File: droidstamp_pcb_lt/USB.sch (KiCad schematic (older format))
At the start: 41 parts, among them J2 USB_2A, J3 USB_2A, P4 CONN_4X2, U4 GL850G, U5 RCLAMP0502B, U6 RCLAMP0502B, U7 RCLAMP0502B, U8 RCLAMP0502B, X2 12MHz

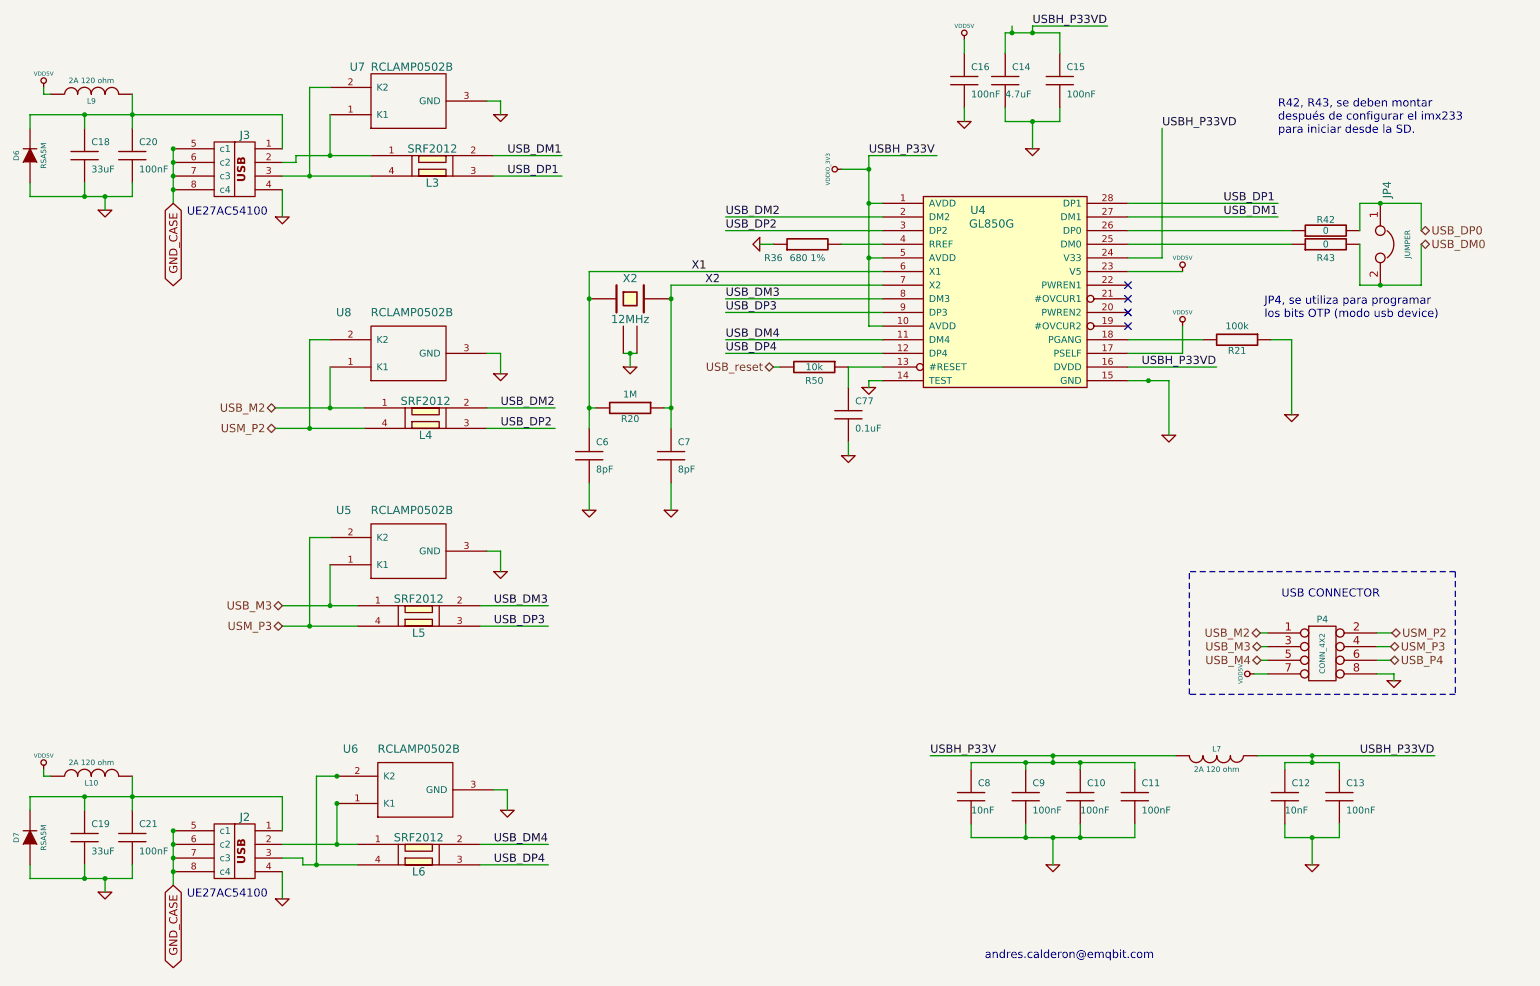
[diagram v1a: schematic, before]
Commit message: USB PC compatible connector
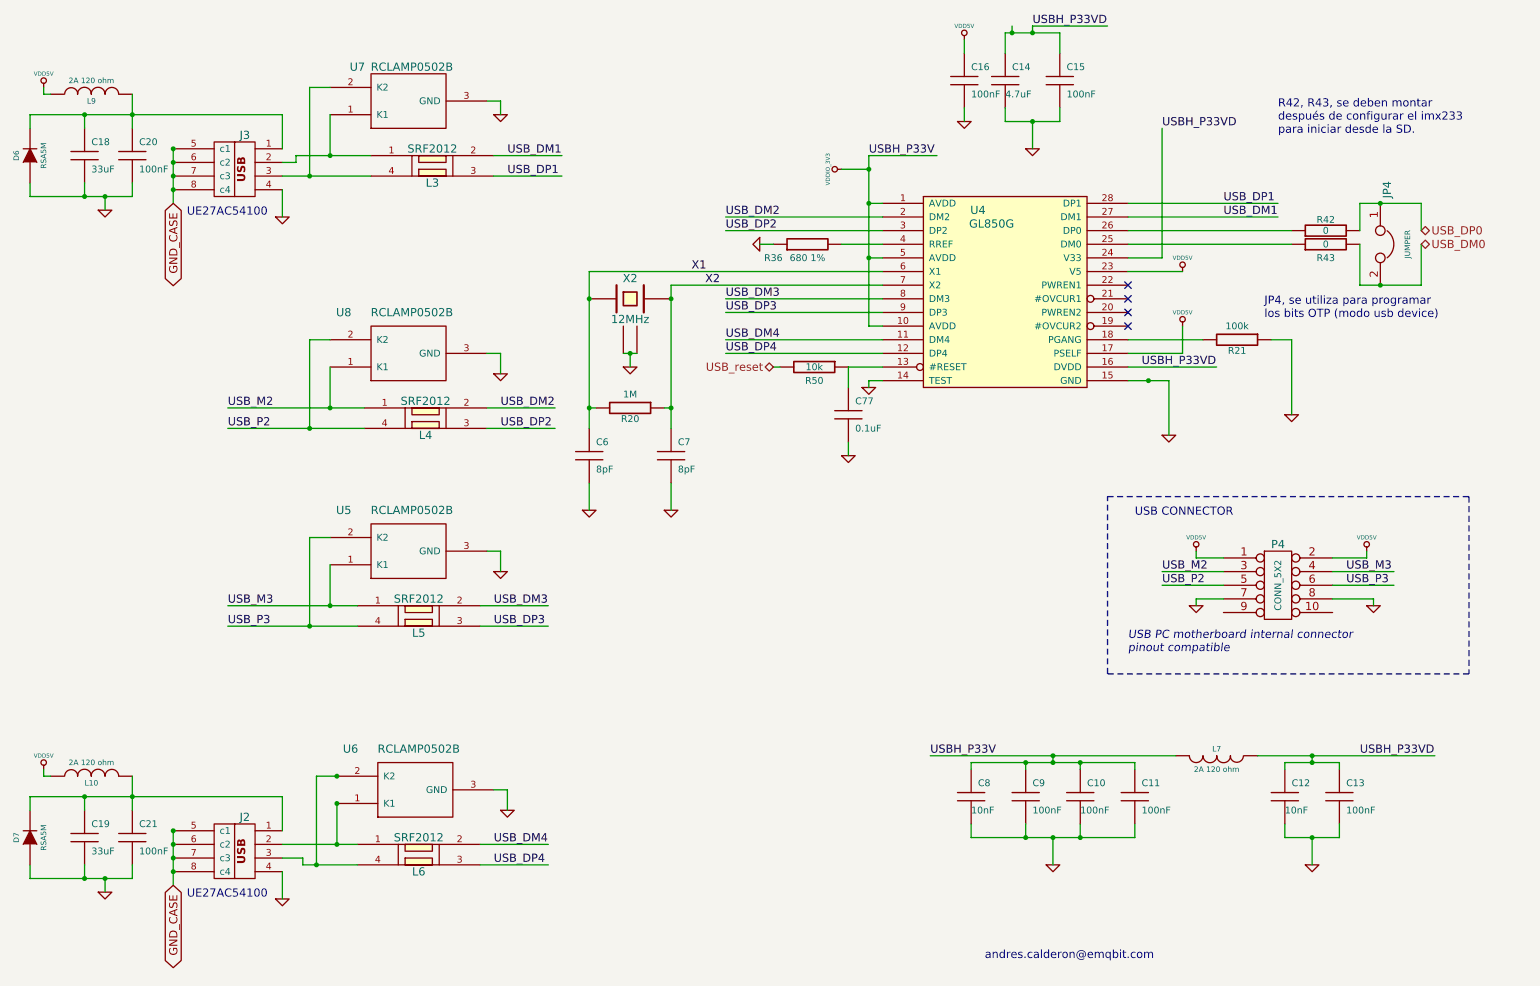
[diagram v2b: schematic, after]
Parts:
- removed P4: CONN_4X2, CONN_4X2, symbol CONN_4X2
- added P4: CONN_5X2, PIN_ARRAY_5x2, symbol CONN_5X2
- D7: footprint diode-1-SOD123 -> RSA5M
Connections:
- net labels added: USB_P2, USB_P3
- net labels removed: USB_M4, USB_P4, USM_P2, USM_P3
- wire segments 162 -> 165
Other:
- note added: "USB PC motherboard internal connector \npinout compatible"
